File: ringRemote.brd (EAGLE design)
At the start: 14.2 x 23 mm, 25 parts, among them Y1 32.768kHz

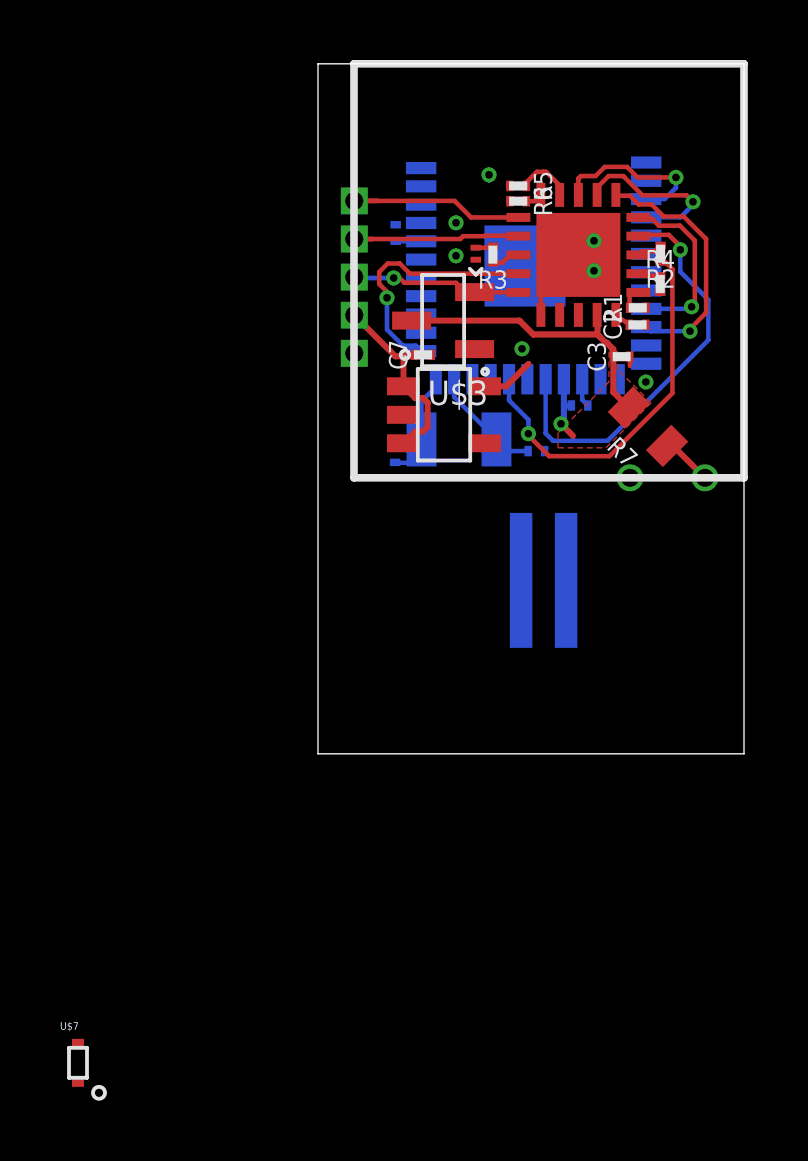
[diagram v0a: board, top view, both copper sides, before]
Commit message: tried to create some vias for the pushbuttons, these need to be routed offboard (past castellated edge near antenna section); created rev1 of mech model (this needs to be bigger and smoother, hurts my finger to wear right now)
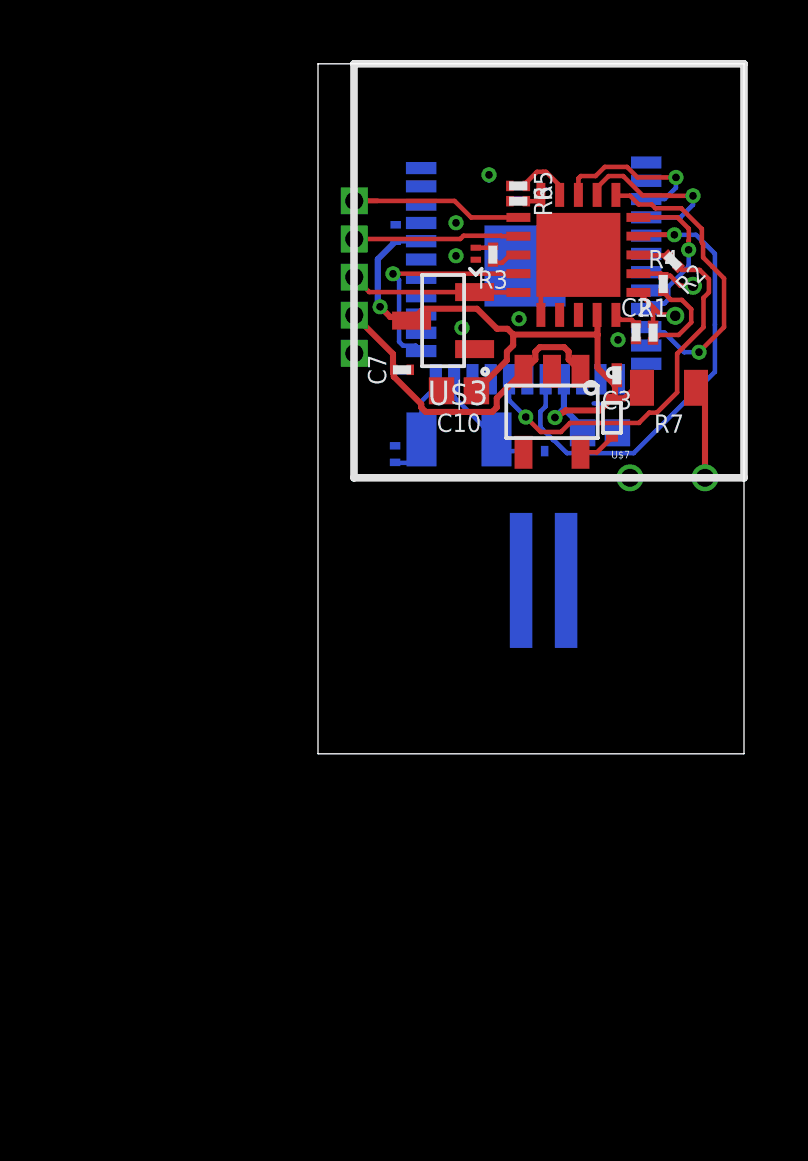
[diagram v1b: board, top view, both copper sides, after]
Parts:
- removed C1: 10uF, ringRemote:0201
- removed FRAME2: FRAME-LETTERNO_PACKAGE, SparkFun-Aesthetics:DUMMY
- added C10, C9: 10uF, ringRemote:0402
- C5, C6: value 1uF -> 4pF
- moved U$7 27.9 mm to (8.60, 11.2), turned to 180 degrees
- moved U$4 3.60 mm to (6.60, 11.4), turned to 180 degrees
- moved R7 1.48 mm to (10.5, 12.2), turned to 180 degrees
- moved R1 0.97 mm to (9.97, 14.0), turned to 0 degrees
- moved C7 0.86 mm to (1.60, 12.8)
- moved C3 0.64 mm to (8.76, 12.6), turned to 180 degrees
- moved R2 0.48 mm to (10.6, 16.4), turned to 225 degrees
- moved C2 0.25 mm to (9.40, 14.1), turned to 0 degrees
- moved R4 0.10 mm to (10.3, 15.7)
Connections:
- removed net VDDIO: C4.1, U$2.P$7
- net GND: now also C10.2, C9.2; no longer C1.2
- net VCC: now also C10.1, C4.1, C9.1, U$2.P$7; no longer C1.1
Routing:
- net VEXT: track 6.47 -> 11.3 mm
- net VCC: track 20.8 -> 24.0 mm, vias 1 -> 2
- net WAKEMONITOR: track 13.8 -> 16.7 mm
- net GND: track 4.75 -> 6.71 mm, vias 8 -> 7
- net VBAT: track 1.70 -> 3.56 mm
- net BT_RTS: track 8.43 -> 10.2 mm
- net PB1: track 0.84 -> 2.45 mm, vias 0 -> 1
- net PB2: track 0.76 -> 1.99 mm, vias 0 -> 1
- net AO_GPIO_0_WAKE: track 8.36 -> 7.39 mm
- net VDDIO: track 0.85 -> 0.00 mm
- net BT_CTS: track 5.99 -> 5.34 mm
- net SWDIO: track 6.11 -> 5.54 mm
- net N$10: track 1.78 -> 1.26 mm
- net MAXRST: track 5.94 -> 6.29 mm, vias 1 -> 0
- removed copper zone on layer 1, net VCC
